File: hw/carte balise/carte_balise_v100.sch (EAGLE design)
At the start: 70 parts, among them IC1 DSPIC33EP512MU810-X_PF, IC2 MCP2551/SN, IC3 MRF24J40MAGND, IC4 MCP2551/SN, M3 DMP2035U, U1 ADXL362

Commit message: rework io connector and start routing the board
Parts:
- removed C21, C22: C_NP_805, etienne:C_NP_805
- removed I/OS, I/OS1, I/OS3: (no value), pinhead-2:PINHD-1X08_2.54
- removed X1: (no value), con-phoenix-254:MPT2
- added C17, C18: 22p-0402, DEVIALET_CAPACITORS:C0402K
- added JP1, JP10, JP11, JP12, JP2, JP3, JP4, JP5, JP6, JP7, JP8, JP9: (no value), pinhead:PINHD-2X3
- added X6: +12V, con-wago-500:W237-102
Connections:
- net CAN1_RX: now also IC1.C3INB/RP70/RD6; no longer IC1.C3INA/VCMPST3/RP71/RD7
- net CAN1_TX: now also IC1.C3INA/VCMPST3/RP71/RD7; no longer IC1.C3INB/RP70/RD6
- net CAN2_RX: now also IC1.PMWR/RP68/RD4; no longer IC1.PMRD/RP69/RD5
- net CAN2_TX: now also IC1.PMRD/RP69/RD5; no longer IC1.PMWR/RP68/RD4
- net GND: now also C17.1, C18.1, JP1.3, JP1.4, JP10.3, JP10.4, JP11.3, JP11.4, JP12.3, JP12.4, JP2.3, JP2.4, JP3.3, JP3.4, JP4.3, JP4.4, JP5.3, JP5.4, JP6.3, JP6.4, JP7.3, JP7.4, JP8.3, JP8.4, JP9.3, JP9.4, X6-2.KL; no longer C21.1, C22.1, X1-1.1
- net N$29: now also C18.2; no longer C22.2
- net N$30: now also C17.2; no longer C21.2
- net N$31: now also X6-1.KL; no longer X1-2.1
- net PIC_RA1: now also JP5.1; no longer I/OS3.1
- net PIC_RA10: now also JP10.2; no longer I/OS.4
- net PIC_RA2: now also JP1.1; no longer I/OS1.4
- net PIC_RA3: now also JP1.2; no longer I/OS1.3
- net PIC_RA4: now also JP2.1; no longer I/OS1.2
- net PIC_RA5: now also JP2.2; no longer I/OS1.1
- net PIC_RA9: now also JP10.1; no longer I/OS.3
- net PIC_RB10: now also JP12.1; no longer I/OS.7
- net PIC_RB11: now also JP12.2; no longer I/OS.8
- net PIC_RB12: now also JP6.2; no longer I/OS3.4
- net PIC_RB13: now also JP7.1; no longer I/OS3.5
- net PIC_RB14: now also JP7.2; no longer I/OS3.6
- net PIC_RB15: now also JP8.1; no longer I/OS3.7
- net PIC_RB6: now also JP9.1; no longer I/OS.1
- net PIC_RB7: now also JP9.2; no longer I/OS.2
- net PIC_RB8: now also JP11.1; no longer I/OS.5
- net PIC_RB9: now also JP11.2; no longer I/OS.6
- net PIC_RD14: now also JP8.2; no longer I/OS3.8
- net PIC_RF12: now also JP6.1; no longer I/OS3.3
- net PIC_RF13: now also JP5.2; no longer I/OS3.2
- net PIC_RF2: now also JP4.1; no longer I/OS1.8
- net PIC_RF8: now also JP4.2; no longer I/OS1.7
- net PIC_RG2: now also JP3.2; no longer I/OS1.5
- net PIC_RG3: now also JP3.1; no longer I/OS1.6
- net UART1_RX: now also IC1.VCPCON/RP65/RD1; no longer IC1.DPH/RP66/RD2
- net UART1_TX: now also IC1.DPH/RP66/RD2; no longer IC1.VCPCON/RP65/RD1
- net V+: now also JP1.5, JP1.6, JP10.5, JP10.6, JP11.5, JP11.6, JP12.5, JP12.6, JP2.5, JP2.6, JP3.5, JP3.6, JP4.5, JP4.6, JP5.5, JP5.6, JP6.5, JP6.6, JP7.5, JP7.6, JP8.5, JP8.6, JP9.5, JP9.6
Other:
- moved on the sheet: I/OS2, IC1, PWM_CON, R18, R19, R20, R21, U$10

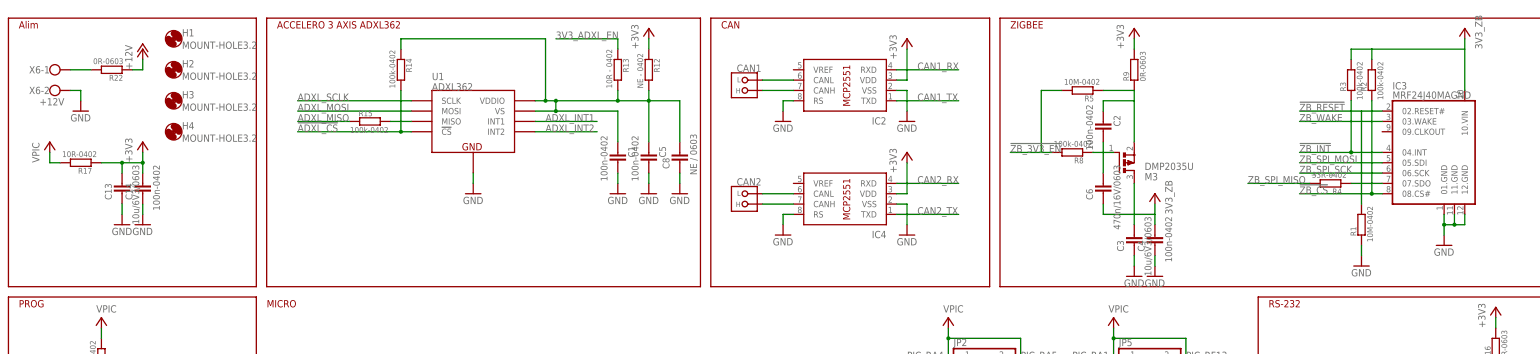
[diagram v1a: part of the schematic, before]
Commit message: wip routing and placement
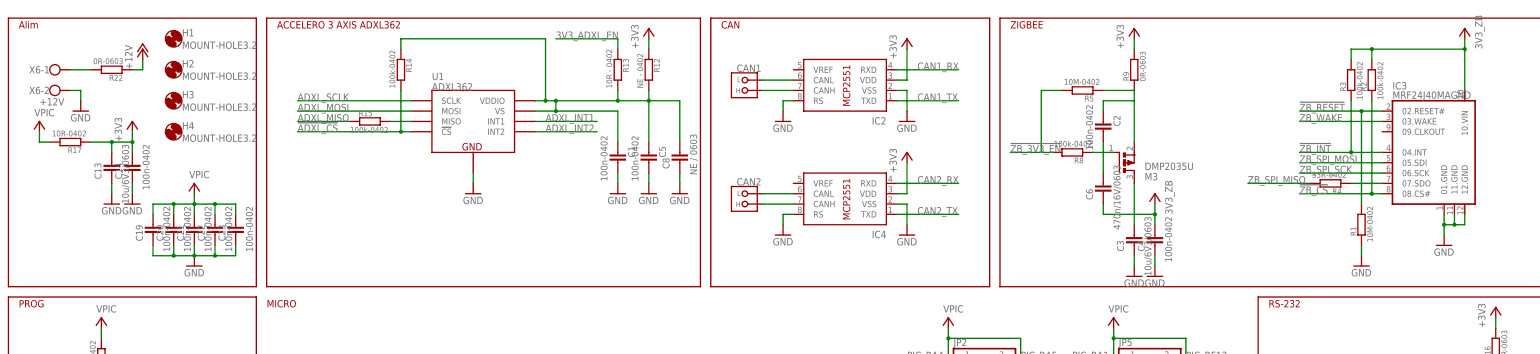
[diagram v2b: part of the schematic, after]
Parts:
- added C19, C20, C21, C22, C23: 100n-0402, DEVIALET_CAPACITORS:C0402K
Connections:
- removed net +3V3P: R16.2, R9.2
- removed net N$10: R2.2, R3.2
- net +3V3: now also R16.2, R9.2; no longer R17.2
- net GND: now also C19.2, C20.2, C21.2, C22.2, C23.2
- net V+: now also C19.1, C20.1, C21.1, C22.1, C23.1, R17.2
- net VDD_RADIO: now also R2.2, R3.2
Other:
- moved on the sheet: C13, C14, R17

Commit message: WIP adxl
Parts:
- removed R20: 33R-0402, DEVIALET_RESISTORS:R0402K
- added R24: 33R-0402, DEVIALET_RESISTORS:R0402K
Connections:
- removed net N$39: IC1.C1IND/SCK2/PMA5/RP118/RG6, R20.1
- new net N$10: IC1.C2IND/SDO2/PMA3/RP120/RG8, R24.1
- net !ADXL_CS: now also IC1.AN19/PWM6H/RP52/RC4; no longer IC1.AN17/PWM5H/RP50/RC2
- net +3V3: now also JP1.5, JP1.6, JP10.5, JP10.6, JP11.5, JP11.6, JP12.5, JP12.6, JP2.5, JP2.6, JP3.5, JP3.6, JP4.5, JP4.6, JP5.5, JP5.6, JP6.5, JP6.6, JP7.5, JP7.6, JP8.5, JP8.6, JP9.5, JP9.6
- net ADXL_INT1: now also IC1.AN16/PWM5L/RP49/RC1; no longer IC1.AN18/PWM6L/RP51/RC3
- net ADXL_INT2: now also IC1.AN17/PWM5H/RP50/RC2; no longer IC1.AN19/PWM6H/RP52/RC4
- net ADXL_MISO: now also IC1.C1IND/SCK2/PMA5/RP118/RG6; no longer IC1.C2IND/SDO2/PMA3/RP120/RG8
- net ADXL_SCLK: now also R24.2; no longer R20.2
- net V+: no longer JP1.5, JP1.6, JP10.5, JP10.6, JP11.5, JP11.6, JP12.5, JP12.6, JP2.5, JP2.6, JP3.5, JP3.6, JP4.5, JP4.6, JP5.5, JP5.6, JP6.5, JP6.6, JP7.5, JP7.6, JP8.5, JP8.6, JP9.5, JP9.6
